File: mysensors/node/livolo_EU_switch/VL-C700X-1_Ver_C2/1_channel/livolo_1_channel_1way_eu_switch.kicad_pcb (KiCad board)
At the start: 2 copper layers, 43 x 43.4 mm, 42 parts, among them CON1 AVR-ISP-6, IC1 ATMEGA328P-AU, P1 Sense Pad 1, P3 ANTENNA, P4 Power Board, U1 MIC5205-3.3, U2 MCP16301, U3 TTP223, U5 RFM69CW, U6 AT25DF512C-SSHN-B, U7 ATSHA204A

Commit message: [mysensors][livolo_EU_switch][VL-C700X-1_Ver_C2][1_channel] initial draft
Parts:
- moved C11 15.8 mm to (133.4, 102.5)
- moved U3 15.8 mm to (133.4, 99.8)
- moved C13 15.8 mm to (133.5, 97.2)
- moved C1 14.9 mm to (132.6, 86.6)
- moved C4 14.9 mm to (122.2, 96.0)
- moved C2 14.9 mm to (122.5, 86.6)
- moved IC1 14.9 mm to (127.5, 91.4)
- moved D6 13.9 mm to (140.7, 102.2)
- moved R6 13.9 mm to (144.4, 103.4)
- moved D5 13.9 mm to (144.1, 102.2)
- moved R5 13.9 mm to (140.3, 103.4)
- moved C6 13.8 mm to (159.0, 98.7)
- moved C7 13.8 mm to (153.4, 99.0)
- moved L1 13.8 mm to (155.8, 94.3)
- moved R3 13.8 mm to (159.0, 94.7)
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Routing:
- net GND: track 142.6 -> 0.00 mm, vias 8 -> 0
- net +3V3: track 131.3 -> 0.00 mm, vias 10 -> 0
- net /SCK: track 52.1 -> 0.00 mm, vias 3 -> 0
- net /MOSI: track 44.3 -> 0.00 mm, vias 2 -> 0
- net /MISO: track 39.8 -> 0.00 mm, vias 4 -> 0
- net /RESET: track 38.6 -> 0.00 mm, vias 2 -> 0
- net /ATSHA204A: track 32.0 -> 0.00 mm, vias 2 -> 0
- net /Relay2_Reset: track 31.5 -> 0.00 mm, vias 1 -> 0
- net /12Vcc: track 27.8 -> 0.00 mm, vias 2 -> 0
- net /S1_LEDs: track 27.6 -> 0.00 mm, vias 2 -> 0
- net /Relay2_Set: track 27.5 -> 0.00 mm, vias 1 -> 0
- net Net-(C7-Pad1): track 21.6 -> 0.00 mm, vias 2 -> 0
- net /FLASH_SS: track 20.3 -> 0.00 mm, vias 2 -> 0
- net /Relay1_Set: track 19.2 -> 0.00 mm, vias 1 -> 0
- net /Relay1_Reset: track 19.0 -> 0.00 mm, vias 1 -> 0
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
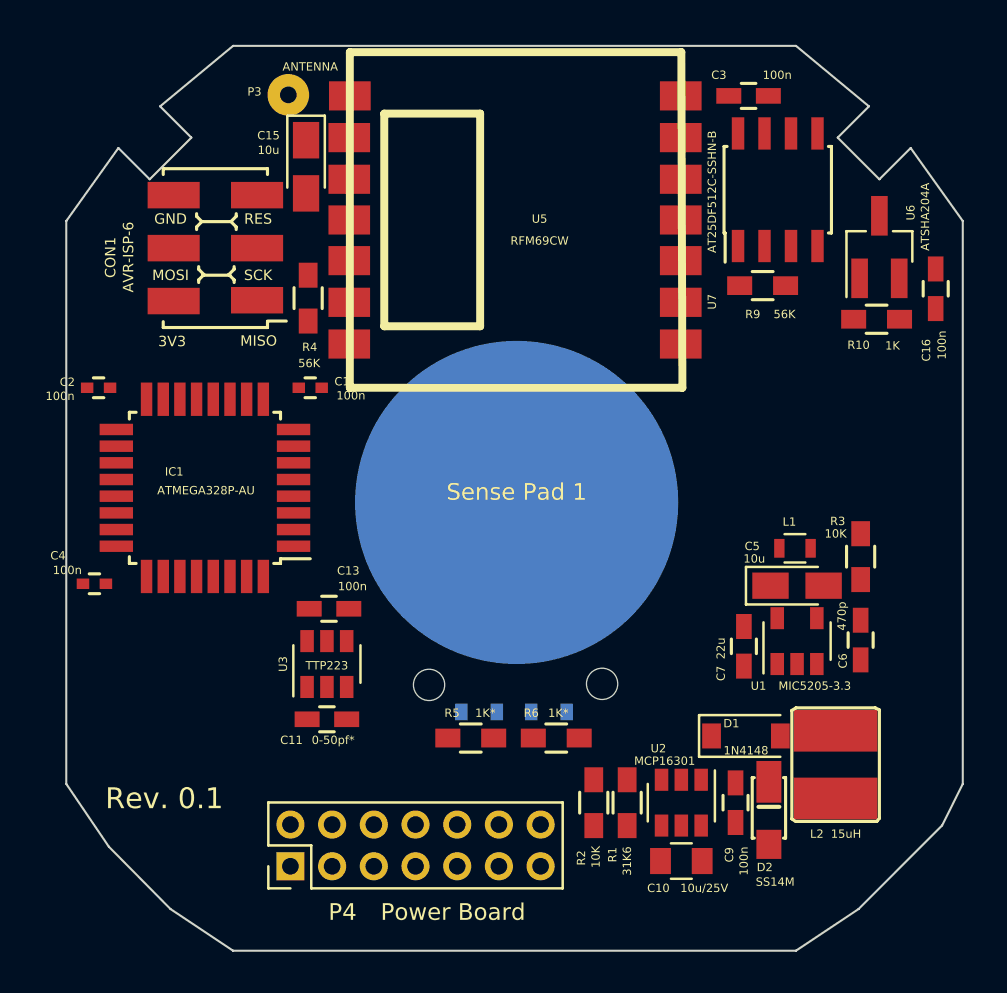
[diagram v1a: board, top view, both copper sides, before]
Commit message: [mysensors][livolo_EU_switch][VL-C700X-1_Ver_C2] pcb refactorings for both 1 & 2 channel variant
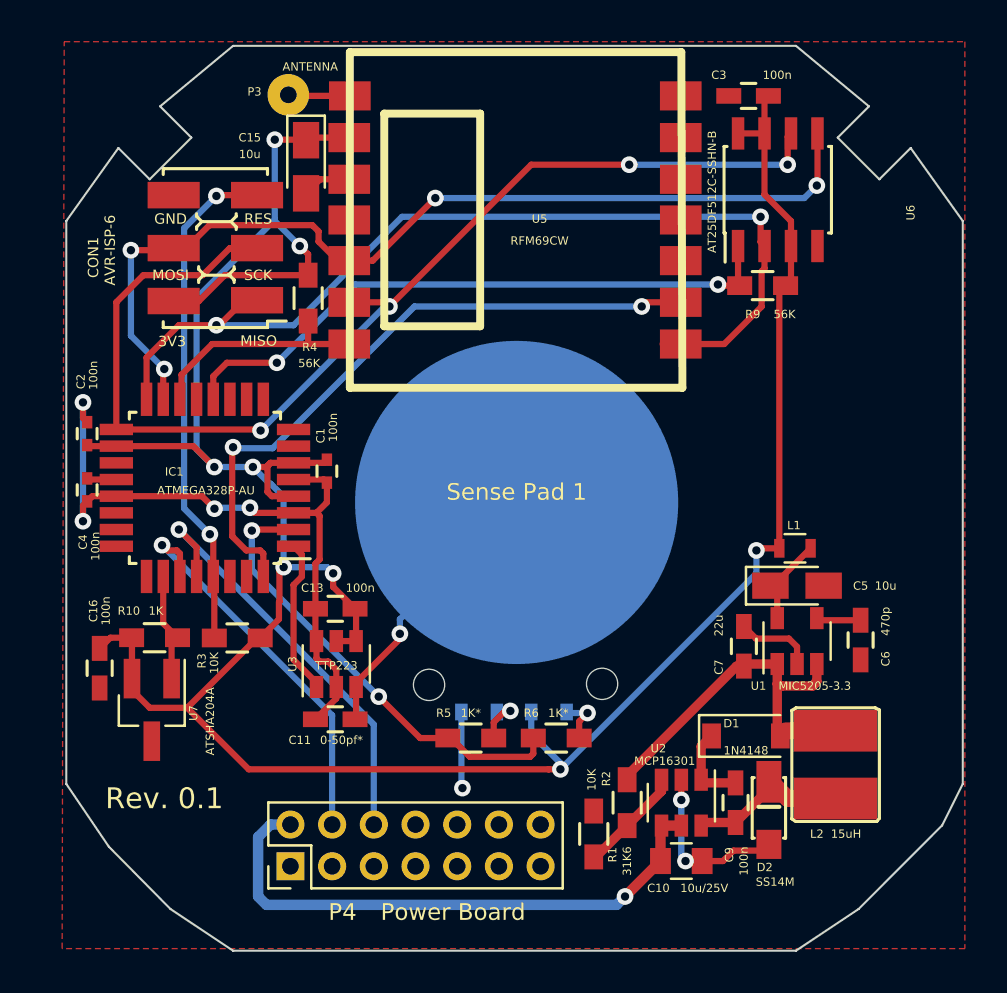
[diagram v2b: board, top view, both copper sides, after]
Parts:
- moved C16 44.0 mm to (122.5, 100.0), turned to 90 degrees
- moved U7 41.4 mm to (125.0, 102.0), turned to 270 degrees
- moved R10 37.9 mm to (125.1, 98.6), turned to 0 degrees
- moved R3 30.2 mm to (129.1, 98.6), turned to 180 degrees
- moved C4 4.51 mm to (121.9, 91.5), turned to 90 degrees
- moved C1 4.08 mm to (133.4, 90.6), turned to 270 degrees
- moved C2 2.27 mm to (121.9, 88.8), turned to 270 degrees
- moved R2 1.50 mm to (146.2, 108.0), turned to 270 degrees
- moved U3 0.45 mm to (133.8, 99.8)
- moved C11 0.40 mm to (133.8, 102.5)
- moved C13 0.30 mm to (133.8, 97.2)
- turned L1 to 0 degrees
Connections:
- IC1 pad 30: /Relay2_Set -> (no net)
- IC1 pad 31: /Relay2_Reset -> (no net)
- P4 pad 3: /Relay2_Reset -> (no net)
- P4 pad 5: /Relay2_Set -> (no net)
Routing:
- net +3V3: track 0.00 -> 136.9 mm, vias 0 -> 8
- net /SCK: track 0.00 -> 55.8 mm, vias 0 -> 4
- net GND: track 0.00 -> 52.0 mm, vias 0 -> 7
- net /MISO: track 0.00 -> 46.6 mm, vias 0 -> 2
- net /MOSI: track 0.00 -> 46.2 mm, vias 0 -> 4
- net /INT: track 0.00 -> 31.6 mm, vias 0 -> 2
- net /FLASH_SS: track 0.00 -> 30.1 mm, vias 0 -> 2
- net /12Vcc: track 0.00 -> 27.7 mm, vias 0 -> 1
- net /RESET: track 0.00 -> 24.4 mm, vias 0 -> 2
- net /S1_LEDs: track 0.00 -> 21.9 mm, vias 0 -> 2
- net /Relay1_Reset: track 0.00 -> 20.6 mm, vias 0 -> 1
- net /Relay1_Set: track 0.00 -> 18.9 mm, vias 0 -> 1
- net Net-(C7-Pad1): track 0.00 -> 18.8 mm
- net Net-(C11-Pad1): track 0.00 -> 13.6 mm, vias 0 -> 1
- net /RADIO_SS: track 0.00 -> 11.0 mm
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- added copper zone on F.Cu, net GND

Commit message: [mysensors]livolo switch nodes - pcb refactorings
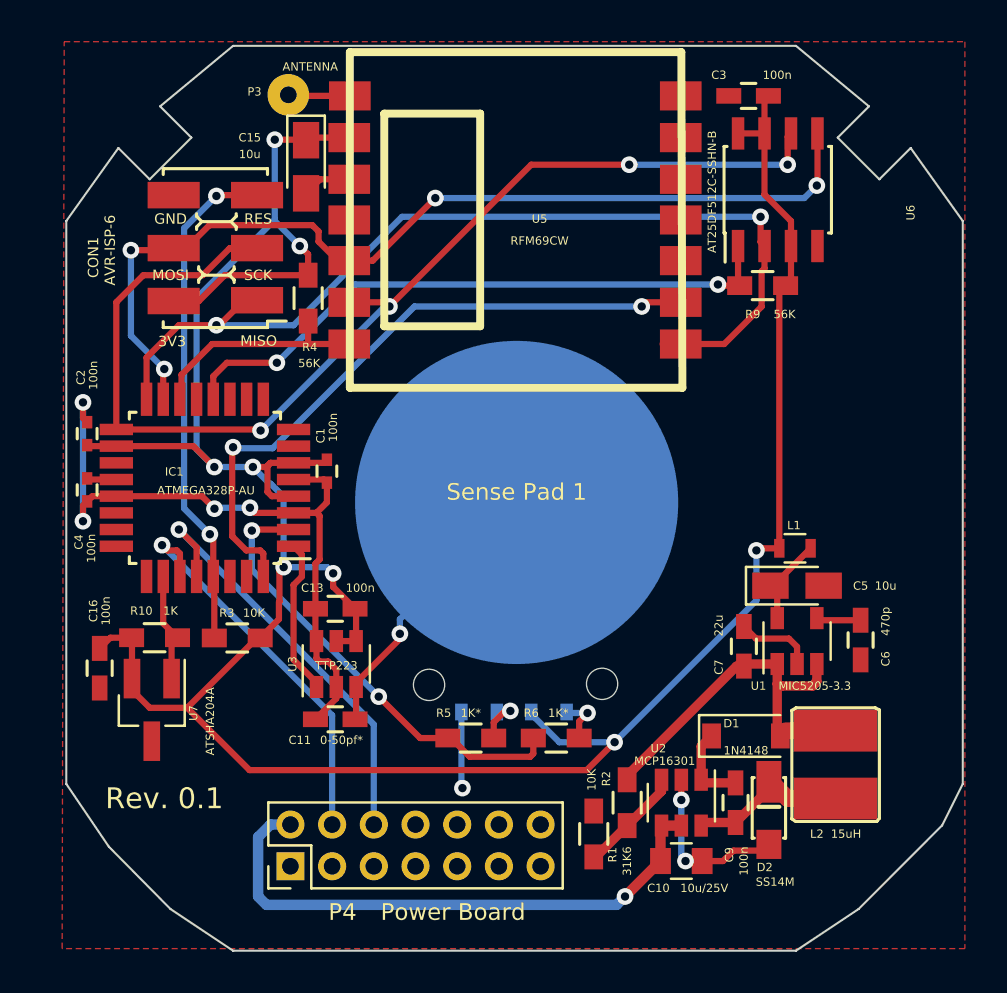
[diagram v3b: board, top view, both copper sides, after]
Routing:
- net +3V3: track 136.9 -> 139.0 mm
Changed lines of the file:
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@@
-(kicad_pcb (version 20170123) (host pcbnew no-vcs-found-4f2ed1b~58~ubuntu16.04.1)
+(kicad_pcb (version 20170123) (host pcbnew no-vcs-found-6cefb68~58~ubuntu16.04.1)
   (general
     (links 96)
@@
     (thickness 1.6)
     (drawings 35)
-    (tracks 361)
+    (tracks 359)
     (zones 0)
     (modules 42)
@@
     (tags "resistor 0603")
     (attr smd)
-    (fp_text reference R3 (at 1.7 -1.1 270) (layer F.SilkS)
-      (effects (font (size 0.4 0.4) (thickness 0.1)))
-    )
-    (fp_text value 10K (at 1.1 -1.2 90) (layer F.SilkS)
+    (fp_text reference R3 (at 0.5 1.2) (layer F.SilkS)
+      (effects (font (size 0.4 0.4) (thickness 0.1)))
+    )
+    (fp_text value 10K (at -0.8 1.2 180) (layer F.SilkS)
       (effects (font (size 0.4 0.4) (thickness 0.1)))
     )
@@
     (tags "resistor 0603")
     (attr smd)
-    (fp_text reference R10 (at -1.234 -1.288) (layer F.SilkS)
-      (effects (font (size 0.4 0.4) (thickness 0.1)))
-    )
-    (fp_text value 1K (at 0.066 -1.288) (layer F.SilkS)
+    (fp_text reference R10 (at -0.634 -1.288) (layer F.SilkS)
+      (effects (font (size 0.4 0.4) (thickness 0.1)))
+    )
+    (fp_text value 1K (at 0.766 -1.288) (layer F.SilkS)
       (effects (font (size 0.4 0.4) (thickness 0.1)))
     )
@@
     (tags "capacitor 0402")
     (attr smd)
-    (fp_text reference C4 (at -2.5 -0.2 270) (layer F.SilkS)
-      (effects (font (size 0.4 0.4) (thickness 0.1)))
-    )
-    (fp_text value 100n (at -2.7 0.4 270) (layer F.SilkS)
+    (fp_text reference C4 (at -2.5 -0.4 270) (layer F.SilkS)
+      (effects (font (size 0.4 0.4) (thickness 0.1)))
+    )
+    (fp_text value 100n (at -2.8 0.2 270) (layer F.SilkS)
       (effects (font (size 0.4 0.4) (thickness 0.1)))
     )
@@
     (tags "capacitor 0402")
     (attr smd)
-    (fp_text reference C2 (at -2.5 0.3 270) (layer F.SilkS)
+    (fp_text reference C2 (at -2.7 0.3 270) (layer F.SilkS)
       (effects (font (size 0.4 0.4) (thickness 0.1)))
     )
@@
     (effects (font (size 1.2 1.2) (thickness 0.2)) (justify mirror))
   )
-  (segment (start 144.6 104.9) (end 144.6 104.6) (width 0.3) (layer B.Cu) (net 1))
-  (segment (start 144.6 104.6) (end 143.2 103.2) (width 0.3) (layer B.Cu) (net 1))
-  (segment (start 143.2 103.2) (end 143.2 102.25) (width 0.3) (layer B.Cu) (net 1) (status 20))
-  (segment (start 143.2 102.25) (end 143.2 102.15) (width 0.3) (layer B.Cu) (net 1) (status 30))
-  (segment (start 144.034311 104.900004) (end 144.034315 104.9) (width 0.3) (layer F.Cu) (net 1))
-  (segment (start 144.034315 104.9) (end 144.6 104.9) (width 0.3) (layer F.Cu) (net 1))
-  (segment (start 154 95.5) (end 144.6 104.9) (width 0.3) (layer B.Cu) (net 1))
-  (segment (start 154 94.4) (end 154 95.5) (width 0.3) (layer B.Cu) (net 1))
-  (segment (start 129.650002 104.900004) (end 144.034311 104.900004) (width 0.3) (layer F.Cu) (net 1))
-  (segment (start 126.699999 101.950001) (end 129.650002 104.900004) (width 0.3) (layer F.Cu) (net 1))
-  (via (at 144.6 104.9) (size 0.8) (drill 0.4) (layers F.Cu B.Cu) (net 1))
+  (segment (start 144.55 103.6) (end 147.2 103.6) (width 0.3) (layer B.Cu) (net 1))
+  (segment (start 143.2 102.25) (end 144.55 103.6) (width 0.3) (layer B.Cu) (net 1) (status 10))
+  (segment (start 145.86128 104.93872) (end 147.2 103.6) (width 0.3) (layer F.Cu) (net 1))
+  (segment (start 129.688718 104.93872) (end 145.86128 104.93872) (width 0.3) (layer F.Cu) (net 1))
+  (segment (start 154 96.8) (end 147.2 103.6) (width 0.3) (layer B.Cu) (net 1))
+  (segment (start 154 94.4) (end 154 96.8) (width 0.3) (layer B.Cu) (net 1))
+  (segment (start 143.2 102.15) (end 143.2 102.25) (width 0.3) (layer B.Cu) (net 1) (status 30))
+  (segment (start 126.699999 101.950001) (end 129.688718 104.93872) (width 0.3) (layer F.Cu) (net 1))
+  (via (at 147.2 103.6) (size 0.8) (drill 0.4) (layers F.Cu B.Cu) (net 1))
   (segment (start 124.034 98.588) (end 123.012 98.588) (width 0.3) (layer F.Cu) (net 1) (status 10))
   (segment (start 123.012 98.588) (end 122.5 99.1) (width 0.3) (layer F.Cu) (net 1) (status 20))

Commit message: [mysensors]livolo switch nodes - pcb refactorings
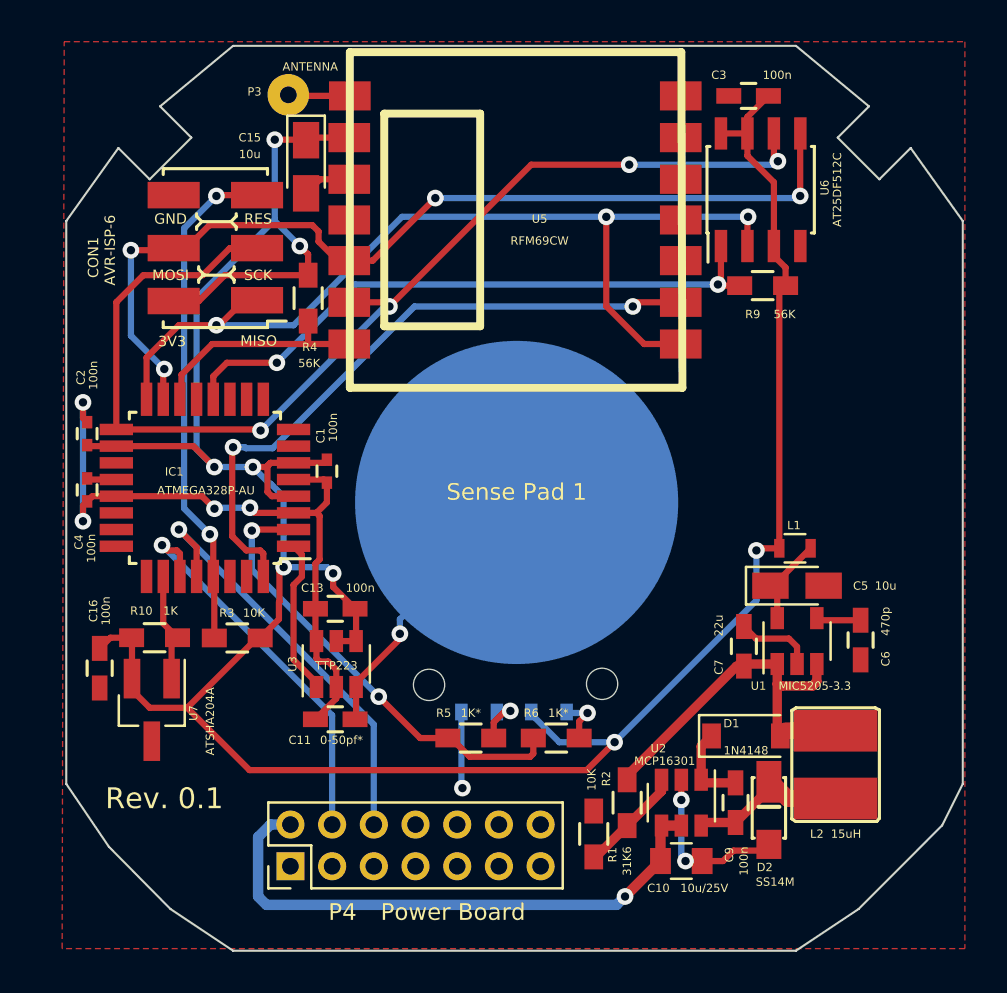
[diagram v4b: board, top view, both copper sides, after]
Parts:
- U6: value AT25DF512C-SSHN-B -> AT25DF512C
- moved U6 0.82 mm to (154.2, 77.1)
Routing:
- net /MISO: track 46.6 -> 47.5 mm, vias 2 -> 3
- net +3V3: track 139.0 -> 139.8 mm
- net /SCK: track 55.8 -> 55.3 mm
- net /MOSI: track 46.2 -> 45.7 mm
